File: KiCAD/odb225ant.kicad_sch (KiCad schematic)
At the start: 13 parts, among them J1 Conn_Coaxial, Q1 BF545A, Q2 BF245A

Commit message: modify readme
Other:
- company: (none) -> JKK & MM
- title: (none) -> PCSK225 Active Antenna
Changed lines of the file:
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@@
 	(generator_version "8.0")
 	(paper "A4")
+	(title_block
+		(title "PCSK225 Active Antenna")
+		(date "2024-04-10")
+		(rev "1.0")
+		(company "JKK & MM")
+	)
 	(junction
 		(at 121.92 67.31)

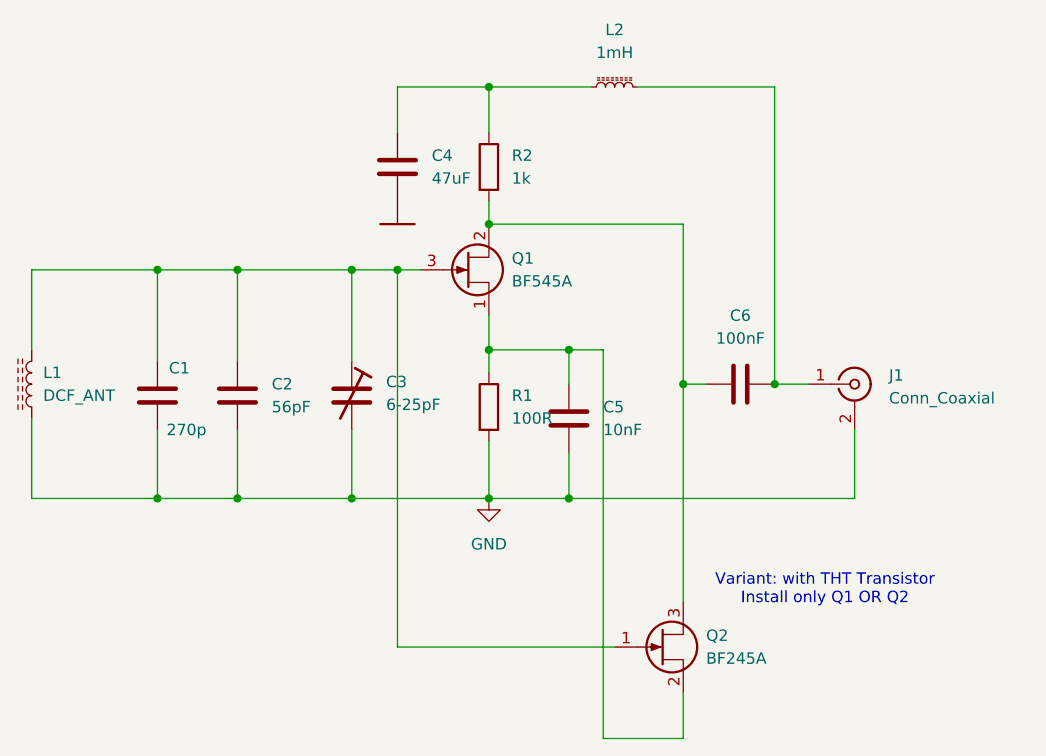
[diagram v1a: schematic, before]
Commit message: fixed C4 GND symbol
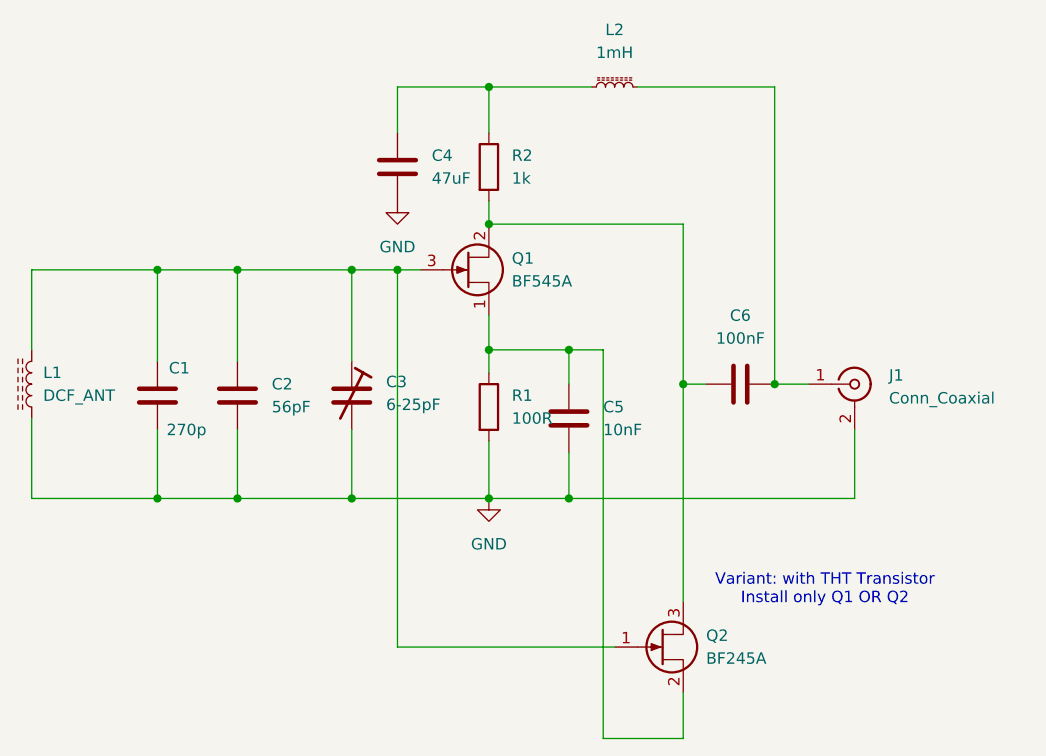
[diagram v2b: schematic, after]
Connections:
- net GND: now also C4.2
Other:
- company: JKK & MM -> (none)
- title: PCSK225 Active Antenna -> (none)
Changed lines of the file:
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@@
 	(generator_version "8.0")
 	(paper "A4")
-	(title_block
-		(title "PCSK225 Active Antenna")
-		(date "2024-04-10")
-		(rev "1.0")
-		(company "JKK & MM")
-	)
 	(junction
 		(at 121.92 67.31)
@@
 	)
 	(symbol
-		(lib_id "odb225:GND")
-		(at 111.76 82.55 0)
-		(unit 1)
-		(exclude_from_sim no)
-		(in_bom yes)
-		(on_board yes)
-		(dnp no)
-		(fields_autoplaced yes)
-		(property "Reference" "#GND01"
-			(at 111.76 82.55 0)
-			(effects
-				(font
-					(size 1.27 1.27)
-				)
-				(hide yes)
-			)
-		)
-		(property "Value" "~"
-			(at 111.76 83.82 0)
-			(effects
-				(font
-					(size 1.778 1.5113)
-				)
-			)
-		)
-		(property "Footprint" ""
-			(at 111.76 82.55 0)
-			(effects
-				(font
-					(size 1.27 1.27)
-				)
-				(hide yes)
-			)
-		)
-		(property "Datasheet" ""
-			(at 111.76 82.55 0)
-			(effects
-				(font
-					(size 1.27 1.27)
-				)
-				(hide yes)
-			)
-		)
-		(property "Description" "SUPPLY SYMBOL"
-			(at 111.76 82.55 0)
-			(effects
-				(font
-					(size 1.27 1.27)
-				)
-				(hide yes)
-			)
-		)
-		(pin "1"
-		)
-		(instances
-			(project "odb225ant"
-				(path "/8dda5e15-4066-419f-a4b8-ba7a35fd4d1c"
-					(reference "#GND01")
-					(unit 1)
-				)
-			)
-		)
-	)
-	(symbol
 		(lib_id "Device:C")
 		(at 93.98 101.6 0)
@@
 					(unit 1)
 				)
+			)
+		)
+	)
+	(symbol
+		(lib_id "power:GND")
+		(at 111.76 80.01 0)
+		(unit 1)
+		(exclude_from_sim no)
+		(in_bom yes)
+		(on_board yes)
+		(dnp no)
+		(fields_autoplaced yes)
+		(property "Reference" "#PWR02"
+			(at 111.76 86.36 0)
+			(effects
+				(font
+					(size 1.27 1.27)
+				)
+				(hide yes)
+			)
+		)
+		(property "Value" "GND"
+			(at 111.76 85.09 0)
+			(effects
+				(font
+					(size 1.27 1.27)
+				)
+			)
+		)
+		(property "Footprint" ""
+			(at 111.76 80.01 0)
+			(effects
+				(font
+					(size 1.27 1.27)
+				)
+				(hide yes)
+			)
+		)
+		(property "Datasheet" ""
+			(at 111.76 80.01 0)
+			(effects
+				(font
+					(size 1.27 1.27)
+				)
+				(hide yes)
+			)
+		)
+		(property "Description" "Power symbol creates a global label with name \"GND\" , ground"
+			(at 111.76 80.01 0)
+			(effects
+				(font
+					(size 1.27 1.27)
+				)
+				(hide yes)
+			)
+		)
+		(pin "1"
+		)
+		(instances
+			(project "odb225ant"
+				(path "/8dda5e15-4066-419f-a4b8-ba7a35fd4d1c"
+					(reference "#PWR02")
+					(unit 1)
+				)
